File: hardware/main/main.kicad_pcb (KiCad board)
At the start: 2 copper layers, 197 parts, among them J101 ST_LINK, J102 USART, J301 Overvoltage_protection, J302 Rad_sensor, J303 Mos_temp, J304 Diode_temp, J601 Supplies, J801 RJ45_Shielded, J802 RJ45_Shielded, Q401 BSC093N15NS5, Q402 BSC093N15NS5, U201 REF3430QDGKRQ1, U202 STM32L431RCTx, U301 INA823DT, U302 INA823DT, U303 INA293A4, U304 INA293A4, U305 TL7726IDR_1, U501 1EDI60N12AF, U601 VXO7805-1000, U602 AMS1117-3.3, U701 MCP2551

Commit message: Layout: Organizing components
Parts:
- F101, L401, Li401, R101, R102, U303, U304: moved to B.Cu
- U301, U302: footprint Package_SO:VSSOP-8_3.0x3.0mm_P0.65mm -> Package_SO:SOIC-8_3.9x4.9mm_P1.27mm
- U305: footprint Package_SON:X2SON-8_1.4x1mm_P0.35mm -> Package_SO:SOIC-8_3.9x4.9mm_P1.27mm
- moved C304 219.9 mm to (365.8, 68.1), turned to -90 degrees
- moved C701 208.3 mm to (302.1, 50.5)
- moved C702 208.3 mm to (289.5, 61.7)
- moved D701 208.3 mm to (290.5, 58.2)
- moved R701 208.3 mm to (298.1, 51.0)
- moved R702 208.3 mm to (298.1, 53.9)
- moved R703 208.3 mm to (296.1, 60.4)
- moved R704 208.3 mm to (300.9, 56.9)
- moved R705 208.3 mm to (296.1, 57.4)
- moved U701 208.3 mm to (291.5, 52.7)
- moved F102 202.1 mm to (230.5, 81.9), turned to 90 degrees
- moved D102 200.8 mm to (233.0, 81.9), turned to -90 degrees
- moved J102 200.2 mm to (234.6, 45.6), turned to -90 degrees
- moved R305 197.7 mm to (367.8, 68.1), turned to 90 degrees
- moved R304 197.6 mm to (367.8, 72.1), turned to -90 degrees
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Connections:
- net /IPanel- renamed /P-
- net Net-(F101-Pad2) renamed /P-Unfused
- C401 pad 1: Net-(C401-Pad1) -> Net-(C403-Pad1)
- C402 pad 1: Net-(C402-Pad1) -> Net-(C403-Pad1)
- C404 pad 1: Net-(C404-Pad1) -> Net-(C403-Pad1)
- C405 pad 1: Net-(C405-Pad1) -> Net-(C408-Pad1)
- C406 pad 1: Net-(C406-Pad1) -> Net-(C408-Pad1)
- C407 pad 1: Net-(C407-Pad1) -> Net-(C408-Pad1)
- D401 pad 2: Net-(C404-Pad1) -> Net-(C403-Pad1)
- D402 pad 2: Net-(C404-Pad1) -> Net-(C403-Pad1)
- D403 pad 2: Net-(C404-Pad1) -> Net-(C403-Pad1)
- D404 pad 2: Net-(C404-Pad1) -> Net-(C403-Pad1)
- R401 pad 2: Net-(C401-Pad1) -> Net-(C403-Pad1)
- R402 pad 2: Net-(C402-Pad1) -> Net-(C403-Pad1)
- R404 pad 2: Net-(C404-Pad1) -> Net-(C403-Pad1)
- R408 pad 2: Net-(C405-Pad1) -> Net-(C408-Pad1)
- R409 pad 2: Net-(C406-Pad1) -> Net-(C408-Pad1)
- R410 pad 2: Net-(C407-Pad1) -> Net-(C408-Pad1)
- U601 pad 1: GND -> /Supplies/+18V
- U601 pad 2: +5V -> GND
- U601 pad 3: /Supplies/+18V -> +5V
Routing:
- net /IBat-: track 0.00 -> 123.0 mm, vias 0 -> 6
- net /Cuk/C: track 0.00 -> 94.0 mm
- net /Cuk/S: track 0.00 -> 53.6 mm
- net /B+: track 0.00 -> 51.6 mm
- net /IPanel+: track 0.00 -> 29.2 mm
- net /B-: track 0.00 -> 11.8 mm
- net /P-Unfused: track 0.00 -> 5.50 mm
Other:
- copper layers 2 -> 4

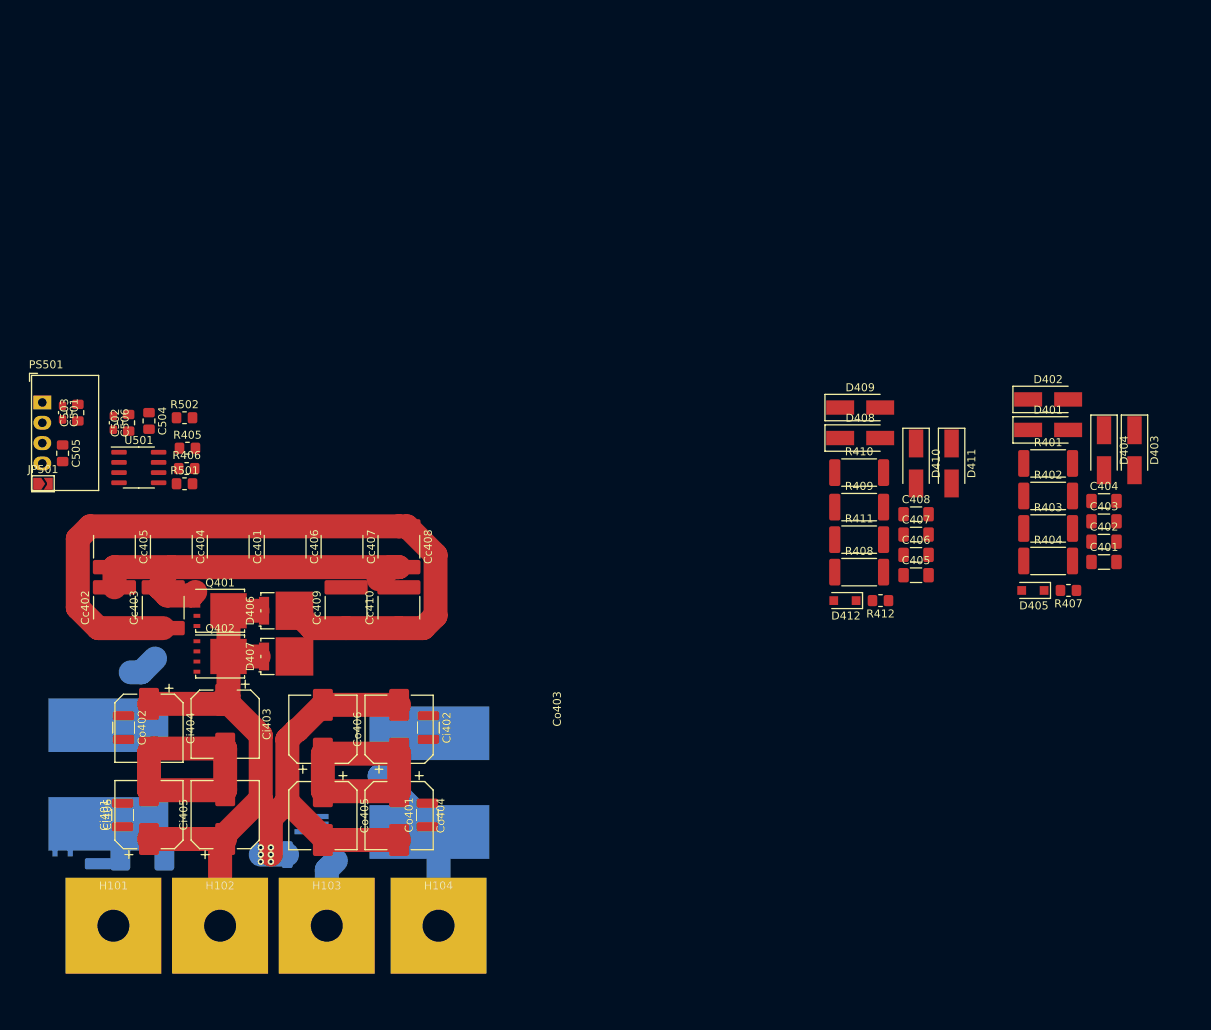
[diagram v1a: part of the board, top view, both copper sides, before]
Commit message: Layout: Organizing power components
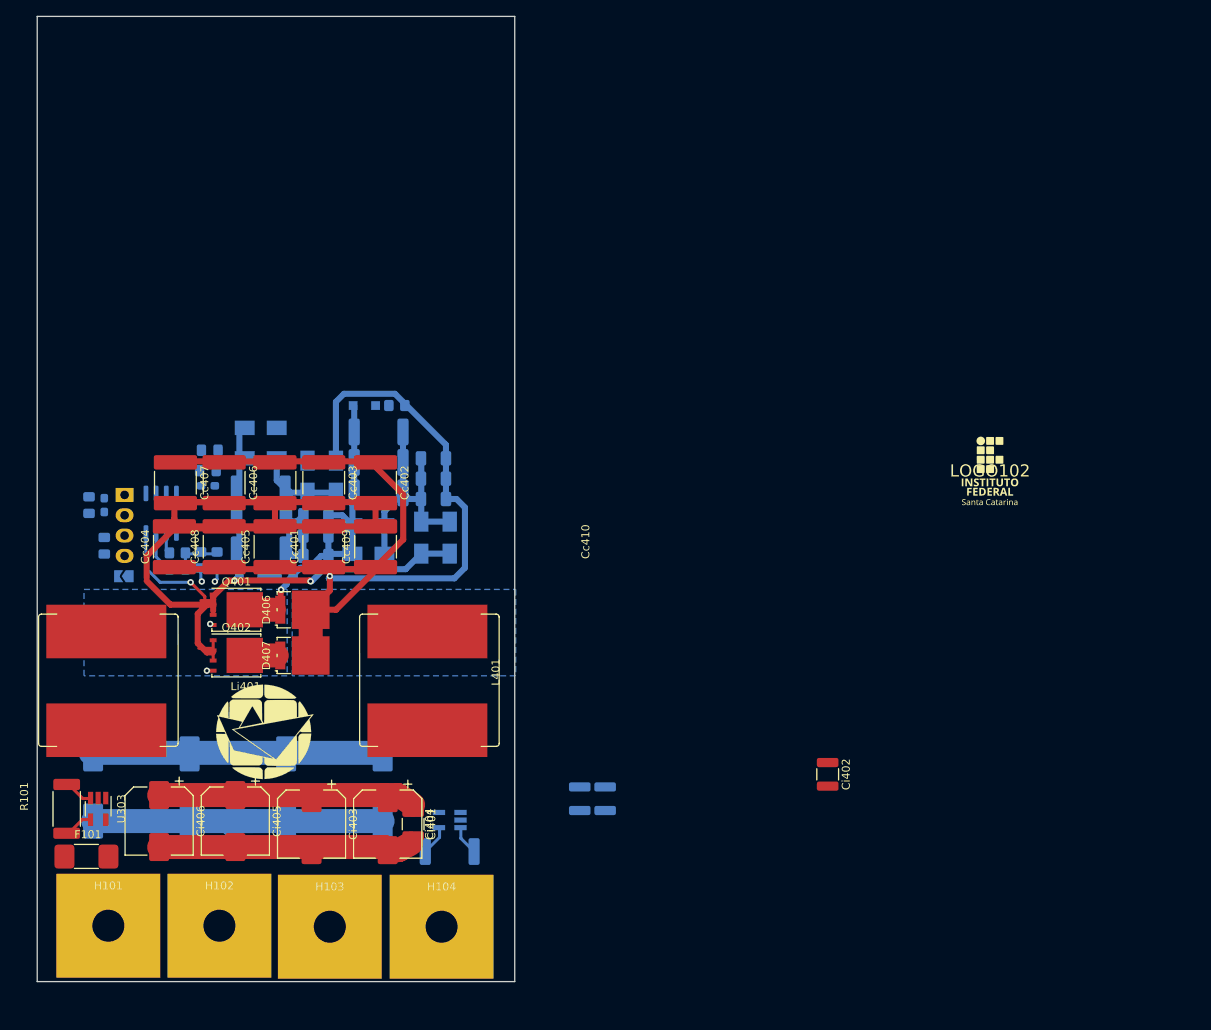
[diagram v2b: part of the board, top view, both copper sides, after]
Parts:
- removed C401, C405: 250V 10nF X7R ±10% 1206, Capacitor_SMD:C_1206_3216Metric_Pad1.33x1.80mm_HandSolder
- removed R401, R408: 2W 200V 10R ±5% 2512, Resistor_SMD:R_2512_6332Metric_Pad1.40x3.35mm_HandSolder
- added LOGO101: Logo_Open_Hardware_Small, Zenite:symbol_logoZenite, F.Cu at (33.5, 88.1)
- added LOGO102: Logo_Open_Hardware_Small, Zenite:synbol_logoifsc, F.Cu at (124.2, 55.5)
- C402, C403, C404, C406, C407, C408, C501, C502, C503, C504, C505, C506, Co401, Co402, D405, D412, JP501, PS501, R402, R403, R404, R405, R406, R407, R409, R410, R411, R412, R501, R502, U501: moved to B.Cu
- Ci403, Ci404, Ci405, Ci406: footprint Capacitor_SMD:CP_Elec_8x6.7 -> Capacitor_SMD:CP_Elec_8x10
- Co403, Co404, Co405, Co406: footprint Capacitor_SMD:CP_Elec_8x6.7 -> Capacitor_SMD:CP_Elec_10x12.5; moved to B.Cu
- D401, D402, D403, D404, D408, D409, D410, D411: footprint Diode_SMD:D_SMA_Handsoldering -> Diode_SMD:D_SMA; moved to B.Cu
- F101, L401, Li401, R101, U303: moved to F.Cu
- H101, H102, H103, H104: footprint Zenite:MountingHole_12mmx12mm_Rectangular -> Zenite:MountingHole_13mmx13mm_Rectangular
- moved D403 103.4 mm to (38.9, 56.3)
- moved R404 98.8 mm to (33.0, 57.8)
- moved C404 98.8 mm to (39.9, 66.2)
- moved D402 98.7 mm to (33.0, 54.0)
- moved R402 98.7 mm to (33.0, 65.4)
- moved C402 98.6 mm to (39.9, 61.1)
- moved C403 98.5 mm to (39.9, 63.6)
- moved R403 98.4 mm to (33.0, 61.6)
- moved D401 98.4 mm to (33.0, 50.2)
- moved R407 97.9 mm to (36.1, 68.6)
- moved D405 97.8 mm to (31.8, 68.6)
- moved D404 96.1 mm to (42.4, 56.3)
- moved D411 66.9 mm to (53.1, 63.9)
- moved R412 65.2 mm to (50.0, 47.4)
- moved D412 64.8 mm to (46.0, 47.4)
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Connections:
- C402 pad 2: /IBat- -> /P+
- C403 pad 2: /IBat- -> /P+
- C404 pad 2: /IBat- -> /P+
- Ci401 pad 1: /IBat- -> /P+
- Ci401 pad 2: /IPanel+ -> /Cuk/IN-
- Ci402 pad 1: /IBat- -> /P+
- Ci402 pad 2: /IPanel+ -> /Cuk/IN-
- Ci403 pad 1: /IBat- -> /P+
- Ci403 pad 2: /IPanel+ -> /Cuk/IN-
- Ci404 pad 1: /IBat- -> /P+
- Ci404 pad 2: /IPanel+ -> /Cuk/IN-
- Ci405 pad 1: /IBat- -> /P+
- Ci405 pad 2: /IPanel+ -> /Cuk/IN-
- Ci406 pad 1: /IBat- -> /P+
- Ci406 pad 2: /IPanel+ -> /Cuk/IN-
- Co401 pad 1: /IBat- -> /P+
- Co402 pad 1: /IBat- -> /P+
- Co403 pad 2: /IBat- -> /P+
- Co404 pad 2: /IBat- -> /P+
- Co405 pad 2: /IBat- -> /P+
- Co406 pad 2: /IBat- -> /P+
- D406 pad 1: /IBat- -> /P+
- D406 pad 2: /IBat- -> /P+
- D407 pad 1: /IBat- -> /P+
- D407 pad 2: /IBat- -> /P+
- D408 pad 1: /IBat- -> /P+
- D409 pad 1: /IBat- -> /P+
- D412 pad 2: /IBat- -> /P+
- H102 pad 1: /IBat- -> /P+
- Li401 pad 2: /IPanel+ -> /Cuk/IN-
- Q401 pad 2: /IBat- -> /P+
- Q402 pad 2: /IBat- -> /P+
- R101 pad 2: /IPanel+ -> /Cuk/IN-
- R102 pad 2: /IBat- -> /P+
- R306 pad 2: /IBat- -> /P+
- R407 pad 1: /IBat- -> /P+
- R409 pad 1: /IBat- -> /P+
- R410 pad 1: /IBat- -> /P+
- R411 pad 1: /IBat- -> /P+
- U303 pad 4: /P- -> /IPanel-
- U304 pad 3: /B- -> /IBat+
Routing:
- net /Cuk/S: track 53.6 -> 182.8 mm, vias 0 -> 3
- net /P+: track 0.00 -> 121.6 mm, vias 0 -> 1
- net /IBat-: track 123.0 -> 3.66 mm, vias 6 -> 0
- net /Cuk/C: track 94.0 -> 149.2 mm, vias 0 -> 1
- net /Cuk/IN-: track 0.00 -> 35.4 mm
- net Net-(C406-Pad1): track 0.00 -> 30.2 mm
- net /IPanel+: track 29.2 -> 0.00 mm
- net Net-(C402-Pad1): track 0.00 -> 28.4 mm
- net /B+: track 51.6 -> 36.2 mm
- net /Cuk/G1: track 0.00 -> 14.6 mm, vias 0 -> 2
- net /Cuk/G0: track 0.00 -> 8.49 mm, vias 0 -> 2
- net /Cuk/driver/OUT_G: track 0.00 -> 6.08 mm
- net /B-: track 11.8 -> 6.16 mm
- net Net-(R502-Pad1): track 0.00 -> 5.32 mm
- net /P-Unfused: track 5.50 -> 9.93 mm
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- added copper zone on B.Cu, net /Cuk/C
- added copper zone on B.Cu, net /P+
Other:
- board outline added: 59.7 x 120.6 mm

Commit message: Layout: Fist version of power stage
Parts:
- added C206: 50V 100nF 0805, Capacitor_SMD:C_0805_2012Metric_Pad1.18x1.45mm_HandSolder, F.Cu at (351.8, 116.6)
- added C207: 50V 100nF 0805, Capacitor_SMD:C_0805_2012Metric_Pad1.18x1.45mm_HandSolder, F.Cu at (347.0, 116.6)
- added C305: 50V 100nF X7R ±10% 0402, Capacitor_SMD:C_0402_1005Metric_Pad0.74x0.62mm_HandSolder, F.Cu at (27.2, 164.7)
- added C306: 50V 100nF X7R ±10% 0402, Capacitor_SMD:C_0402_1005Metric_Pad0.74x0.62mm_HandSolder, B.Cu at (72.4, 168.1)
- added D205: Bat_OverV_Out, LED_SMD:LED_0805_2012Metric_Pad1.15x1.40mm_HandSolder, F.Cu at (322.3, 46.5)
- added H401: Heatsink, MountingHole:MountingHole_3.2mm_M3, F.Cu at (22.6, 142.0)
- added H402: Heatsink, MountingHole:MountingHole_3.2mm_M3, F.Cu at (74.7, 142.2)
- added JP204: ID_0, Zenite:SolderJumper-2_P0.5mm_Open_TrianglePad0.5x0.5mm, F.Cu at (331.2, 46.7)
- added JP205: ID_1, Zenite:SolderJumper-2_P0.5mm_Open_TrianglePad0.5x0.5mm, F.Cu at (322.1, 52.7)
- added JP206: ID_2, Zenite:SolderJumper-2_P0.5mm_Open_TrianglePad0.5x0.5mm, F.Cu at (326.8, 50.3)
- added JP207: ID_3, Zenite:SolderJumper-2_P0.5mm_Open_TrianglePad0.5x0.5mm, F.Cu at (326.9, 46.7)
- added JP502: Enable_Driver_5V, Zenite:SolderJumper-2_P0.5mm_Open_TrianglePad0.5x0.5mm, B.Cu at (28.7, 126.6)
- added NT101: NetTie_2, Resistor_SMD:R_0201_0603Metric, F.Cu at (359.1, 122.8)
- added NT102: NetTie_2, Resistor_SMD:R_0201_0603Metric, F.Cu at (361.6, 124.5)
- added NT103: Resistor_SMD:R_0201_0603Metric, Resistor_SMD:R_0201_0603Metric, F.Cu at (361.6, 122.8)
- added NT104: NetTie_2, Resistor_SMD:R_0201_0603Metric, F.Cu at (359.1, 124.5)
- added R208: 1kR 0805, Resistor_SMD:R_0805_2012Metric_Pad1.20x1.40mm_HandSolder, F.Cu at (322.3, 49.5)
- added R322: NC, Resistor_SMD:R_0805_2012Metric_Pad1.20x1.40mm_HandSolder, F.Cu at (291.6, 100.2)
- added R323: NC, Resistor_SMD:R_0805_2012Metric_Pad1.20x1.40mm_HandSolder, F.Cu at (286.8, 100.2)
- added R324: ?, Resistor_SMD:R_0805_2012Metric_Pad1.20x1.40mm_HandSolder, F.Cu at (291.6, 103.1)
- added R325: ?, Resistor_SMD:R_0805_2012Metric_Pad1.20x1.40mm_HandSolder, F.Cu at (286.8, 103.1)
- added REF**: R_0201_0603Metric, Resistor_SMD:R_0201_0603Metric, F.Cu at (357.4, 107.2)
- added TP203: Timer_Break, TestPoint:TestPoint_Pad_2.0x2.0mm, F.Cu at (331.0, 50.5)
- JP101, JP102, JP103, JP104, JP105, JP106, JP107, JP108, JP109, JP110, JP201, JP202, JP301, JP302, JP303, JP304, JP501: footprint Jumper:SolderJumper-2_P1.3mm_Open_TrianglePad1.0x1.5mm -> Zenite:SolderJumper-2_P0.5mm_Open_TrianglePad0.5x0.5mm
- JP203: footprint Jumper:SolderJumper-3_P1.3mm_Open_Pad1.0x1.5mm -> Jumper:SolderJumper-3_P2.0mm_Open_TrianglePad1.0x1.5mm
- moved R307 332.2 mm to (20.1, 136.1), turned to -90 degrees
- moved R306 330.5 mm to (22.1, 136.1), turned to -90 degrees
- moved R311 327.8 mm to (21.1, 133.1), turned to 0 degrees
- moved R312 325.1 mm to (20.1, 130.0), turned to 90 degrees
- moved R310 323.5 mm to (22.1, 130.0), turned to -90 degrees
- moved R316 294.0 mm to (19.8, 117.9), turned to -90 degrees
- moved R318 285.9 mm to (23.4, 112.8), turned to 180 degrees
- moved C309 285.7 mm to (23.4, 110.7), turned to 0 degrees
- moved U301 285.4 mm to (26.4, 131.1), turned to 90 degrees
- moved U202 214.8 mm to (61.2, 105.2)
- moved J802 208.3 mm to (73.9, 86.6)
- moved J801 206.9 mm to (55.0, 86.6)
- moved J102 197.1 mm to (40.3, 78.8)
- moved J101 196.5 mm to (27.4, 70.3), turned to 0 degrees
- moved D101 195.9 mm to (29.5, 88.9)
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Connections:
- C402 pad 2: /P+ -> /Cuk/A
- C403 pad 2: /P+ -> /Cuk/A
- C404 pad 2: /P+ -> /Cuk/A
- C503 pad 1: /5V_Driver -> Net-(C503-Pad1)
- Ci401 pad 1: /P+ -> /Cuk/A
- Ci401 pad 2: /Cuk/IN- -> /P-
- Ci402 pad 1: /P+ -> /Cuk/A
- Ci402 pad 2: /Cuk/IN- -> /P-
- Ci403 pad 1: /P+ -> /Cuk/A
- Ci403 pad 2: /Cuk/IN- -> /P-
- Ci404 pad 1: /P+ -> /Cuk/A
- Ci404 pad 2: /Cuk/IN- -> /P-
- Ci405 pad 1: /P+ -> /Cuk/A
- Ci405 pad 2: /Cuk/IN- -> /P-
- Ci406 pad 1: /P+ -> /Cuk/A
- Ci406 pad 2: /Cuk/IN- -> /P-
- Co401 pad 1: /P+ -> /Cuk/A
- Co402 pad 1: /P+ -> /Cuk/A
- Co403 pad 2: /P+ -> /Cuk/A
- Co404 pad 2: /P+ -> /Cuk/A
- Co405 pad 2: /P+ -> /Cuk/A
- Co406 pad 2: /P+ -> /Cuk/A
- D406 pad 1: /P+ -> /Cuk/A
- D406 pad 2: /P+ -> /Cuk/A
- D407 pad 1: /P+ -> /Cuk/A
- D407 pad 2: /P+ -> /Cuk/A
- D408 pad 1: /P+ -> /Cuk/A
- D409 pad 1: /P+ -> /Cuk/A
- D412 pad 2: /P+ -> /Cuk/A
- F101 pad 1: /P- -> /P+
- F101 pad 2: /P-Unfused -> /P+Unfused
- H101 pad 1: /P-Unfused -> /P-
- H102 pad 1: /P+ -> /P+Unfused
- J301 pad 3: /Analog/Overvoltage_interrupt -> /Analog/Vbat_comp_in_EXT
- Li401 pad 2: /Cuk/IN- -> /P-
- Q401 pad 2: /P+ -> /Cuk/A
- Q402 pad 2: /P+ -> /Cuk/A
- R101 pad 1: /P- -> /P+
- R101 pad 2: /Cuk/IN- -> /Cuk/A
- R102 pad 2: /P+ -> /Cuk/A
- R407 pad 1: /P+ -> /Cuk/A
- R409 pad 1: /P+ -> /Cuk/A
- R410 pad 1: /P+ -> /Cuk/A
- R411 pad 1: /P+ -> /Cuk/A
- U202 pad 10: /Analog/V_bat_adc+ -> /Analog/V_panel_adc+
- U202 pad 11: GND -> unconnected-(U202-Pad11)
- U202 pad 16: /Analog/V_panel_adc+ -> /Analog/Vbat_comp
- U202 pad 17: GND -> /Analog/V_bat_adc+
- U202 pad 23: unconnected-(U202-Pad23) -> /STM32/Bat_OverV_Out
- U202 pad 24: unconnected-(U202-Pad24) -> /Analog/Vbat_comp_in_EXT
- U202 pad 25: unconnected-(U202-Pad25) -> /Analog/Vbat_comp_EXT
- U202 pad 33: /Analog/Overvoltage_interrupt -> Net-(U202-Pad33)
- U202 pad 58: unconnected-(U202-Pad58) -> Net-(U202-Pad58)
- U202 pad 59: unconnected-(U202-Pad59) -> Net-(U202-Pad59)
- U202 pad 61: unconnected-(U202-Pad61) -> Net-(U202-Pad61)
- U202 pad 62: unconnected-(U202-Pad62) -> Net-(U202-Pad62)
- U202 pad 9: GND -> unconnected-(U202-Pad9)
- U501 pad 1: /5V_Driver -> Net-(C503-Pad1)
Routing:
- net /Cuk/S: track 182.8 -> 94.9 mm
- net /P+: track 121.6 -> 37.1 mm, vias 1 -> 74
- net /Cuk/A: track 0.00 -> 75.7 mm, vias 0 -> 353
- net /Cuk/C: track 149.2 -> 76.0 mm, vias 1 -> 585
- net /P-: track 3.57 -> 48.4 mm, vias 0 -> 382
- net /Cuk/IN-: track 35.4 -> 0.00 mm
- net GND: track 0.00 -> 30.3 mm, vias 0 -> 2
- net /B-: track 6.16 -> 27.4 mm
- net Net-(C503-Pad1): track 0.00 -> 13.7 mm
- net Net-(C402-Pad1): track 28.4 -> 41.4 mm
- net /Cuk/driver/+15V_isolated: track 0.00 -> 11.7 mm
- net /P-Unfused: track 9.93 -> 0.00 mm
- net /Analog/3V3_IPanel: track 0.00 -> 6.37 mm, vias 0 -> 1
- net Net-(R307-Pad1): track 0.00 -> 6.15 mm
- net Net-(R306-Pad1): track 0.00 -> 6.15 mm
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- added copper zone on B.Cu, net /B+
- added copper zone on F.Cu, net /B+
- added copper zone on B.Cu, net /B-
- added copper zone on B.Cu, net /Cuk/A
- added copper zone on F.Cu, net /Cuk/A
- added copper zone on F.Cu, net /Cuk/C
- added copper zone on B.Cu, net /Cuk/S
- added copper zone on F.Cu, net /Cuk/S
- added copper zone on F.Cu, net /P+
- added copper zone on B.Cu, net /P+Unfused
- added copper zone on F.Cu, net /P+Unfused
- added copper zone on In1.Cu, net /P+Unfused
- added copper zone on In2.Cu, net /P+Unfused
- added copper zone on B.Cu, net /P-
- added copper zone on F.Cu, net /P-
- added copper zone on In1.Cu, net /P-
- added copper zone on In2.Cu, net /P-
- added copper zone on B.Cu, net Net-(C402-Pad1)
- added copper zone on B.Cu, net Net-(C406-Pad1)
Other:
- board size 59.7 x 120.6 mm -> 59.7 x 120.7 mm
- board text added: "B+"
- board text added: "B-"
- board text added: "P+"
- board text added: "P-"

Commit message: Layout: oganizing components of Driver and voltage sensors
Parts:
- C605, C606, J601, U602: moved to B.Cu
- moved U305 320.5 mm to (47.8, 110.2)
- moved R308 278.5 mm to (73.4, 135.9), turned to -90 degrees
- moved R309 277.0 mm to (75.4, 135.9), turned to -90 degrees
- moved R313 274.6 mm to (71.4, 135.9), turned to -90 degrees
- moved R314 274.2 mm to (74.4, 133.1), turned to 180 degrees
- moved R315 269.0 mm to (77.5, 135.9), turned to 90 degrees
- moved C206 225.7 mm to (135.0, 179.5)
- moved C207 225.7 mm to (130.2, 179.5)
- moved C302 225.7 mm to (113.1, 166.7)
- moved C305 225.7 mm to (109.1, 139.9)
- moved C306 225.7 mm to (119.9, 160.8)
- moved C308 225.7 mm to (102.3, 169.9)
- moved C314 225.7 mm to (102.3, 172.9)
- moved D205 225.7 mm to (105.5, 109.4)
- moved D303 225.7 mm to (138.0, 160.8)
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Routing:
- net /P-: track 48.4 -> 63.8 mm, vias 382 -> 383
- net Net-(C502-Pad1): track 4.48 -> 15.4 mm
- net GND: track 30.3 -> 39.7 mm
- net Net-(R316-Pad2): track 0.00 -> 7.66 mm
- net /5V_Driver: track 4.22 -> 10.8 mm
- net Net-(R308-Pad1): track 0.00 -> 4.67 mm
- net Net-(R309-Pad1): track 0.00 -> 4.66 mm
- net Net-(C503-Pad1): track 13.7 -> 9.38 mm
- net /Cuk/S: track 94.9 -> 91.5 mm, vias 3 -> 13
- net Net-(R316-Pad1): track 0.00 -> 2.82 mm
- net /Cuk/driver/+15V_isolated: track 11.7 -> 9.34 mm
- net /P+: track 37.1 -> 38.2 mm, vias 74 -> 75
- net Net-(R306-Pad1): track 6.15 -> 6.68 mm

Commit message: Layout: Organize and initialize routing of control
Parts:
- removed the C206 at (131.9, 81.2)
- removed the C207 at (147.5, 72.3)
- removed the C305 at (109.1, 139.9)
- removed the C306 at (119.9, 160.8)
- removed NT101, NT102, NT104: NetTie_2, Resistor_SMD:R_0201_0603Metric
- removed NT103: Resistor_SMD:R_0201_0603Metric, Resistor_SMD:R_0201_0603Metric
- removed REF**: R_0201_0603Metric, Resistor_SMD:R_0201_0603Metric
- added C315: 50V 100nF 0805, Capacitor_SMD:C_0805_2012Metric_Pad1.18x1.45mm_HandSolder, F.Cu at (32.7, 90.5)
- added D308: ESD351DPYR, Diode_SMD:D_0402_1005Metric_Pad0.77x0.64mm_HandSolder, F.Cu at (32.4, 92.2)
- added R326: ?, Resistor_SMD:R_0805_2012Metric_Pad1.20x1.40mm_HandSolder, F.Cu at (32.7, 88.4)
- added TH303: NTC 10k 1SDNT2012X103F3950FTF, Resistor_SMD:R_0805_2012Metric_Pad1.20x1.40mm_HandSolder, F.Cu at (32.7, 84.6)
- added TP401: G0, TestPoint:TestPoint_Pad_1.5x1.5mm, F.Cu at (39.6, 142.7)
- added TP402: G1, TestPoint:TestPoint_Pad_1.5x1.5mm, F.Cu at (41.9, 151.9)
- added TP403: D, TestPoint:TestPoint_Pad_1.5x1.5mm, F.Cu at (49.8, 151.1)
- added TP404: S, TestPoint:TestPoint_Pad_1.5x1.5mm, F.Cu at (36.6, 142.7)
- added TP405: C, TestPoint:TestPoint_Pad_1.5x1.5mm, F.Cu at (58.4, 142.2)
- added TP406: A, TestPoint:TestPoint_Pad_1.5x1.5mm, F.Cu at (45.7, 151.1)
- C201, C202, C203, C204, C301, C303, C304, C313, C314, C701, C702, D101, D201, D202, D203, D204, D205, D302, D303, D701, J101, J801, J802, JP101, JP102, JP103, JP104, JP105, JP106, JP109, JP110, JP202, JP203, JP303, JP304, R204, R205, R206, R207, R208, R301, R303, R304, R305, R701, R702, R703, R704, R705, TP201, TP202, TP203, U201, U305, U701: moved to B.Cu
- J601: moved to F.Cu
- moved C310 174.1 mm to (22.6, 113.5)
- moved R319 173.4 mm to (22.6, 115.6)
- moved J301 143.6 mm to (35.2, 115.8), turned to 90 degrees
- moved R320 135.0 mm to (22.3, 109.2), turned to 90 degrees
- moved JP106 133.0 mm to (26.2, 134.6), turned to -90 degrees
- moved D204 132.2 mm to (20.9, 100.5)
- moved C206 132.1 mm to (30.0, 99.3), turned to -90 degrees
- moved C311 129.3 mm to (24.3, 109.2), turned to -90 degrees
- moved D202 128.1 mm to (20.9, 105.0)
- moved R207 127.6 mm to (24.8, 100.5), turned to 180 degrees
- moved C211 124.6 mm to (29.5, 107.7), turned to -90 degrees
- moved R701 124.2 mm to (43.2, 106.7), turned to 90 degrees
- moved R204 123.8 mm to (24.8, 107.3), turned to 180 degrees
- moved D306 122.5 mm to (22.6, 112.0)
- moved R704 122.4 mm to (47.7, 112.3), turned to -90 degrees
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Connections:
- D306 pad 2: /Analog/I_panel_adc+ -> /Analog/V_bat_adc+
- U202 pad 9: unconnected-(U202-Pad9) -> /Analog/V_temp_amb
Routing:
- net GND: track 39.7 -> 403.5 mm, vias 2 -> 9
- net /Analog/V_bat_unfiltered+: track 0.00 -> 62.9 mm
- net /can_connector/CAN_L: track 0.00 -> 39.3 mm
- net /STM32/USART_TX: track 0.00 -> 33.0 mm
- net /STM32/USART_RX: track 0.00 -> 31.4 mm
- net /can_connector/CAN_18V: track 0.00 -> 31.3 mm
- net /can_connector/CAN_H: track 0.00 -> 29.1 mm
- net +3V3: track 0.00 -> 24.1 mm
- net /Analog/V_temp_diode: track 0.00 -> 23.7 mm
- net /Analog/Vbat_comp_EXT: track 0.00 -> 21.6 mm
- net /can/CAN_H: track 0.00 -> 20.5 mm
- net +5V: track 0.00 -> 18.3 mm, vias 0 -> 1
- net /can/CAN_L: track 0.00 -> 16.8 mm
- net /Analog/I_bat_adc+: track 0.00 -> 13.7 mm
- net /STM32/3V_Ref: track 0.00 -> 13.2 mm
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- added copper zone on B.Cu, net +3V3
- added copper zone on B.Cu, net GND
- added copper zone on F.Cu, net GND
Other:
- board size 59.7 x 120.7 mm -> 59.7 x 109.5 mm
